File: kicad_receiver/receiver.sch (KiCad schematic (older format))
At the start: 48 parts, among them J1 Conn_01x05_Male, J2 M1+, J3 M1-, J4 M2+, J5 M2-, J6 CHG+5V, J7 CHG-, J8 BAT+, J9 BAT-, U1 LP2985-3.3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

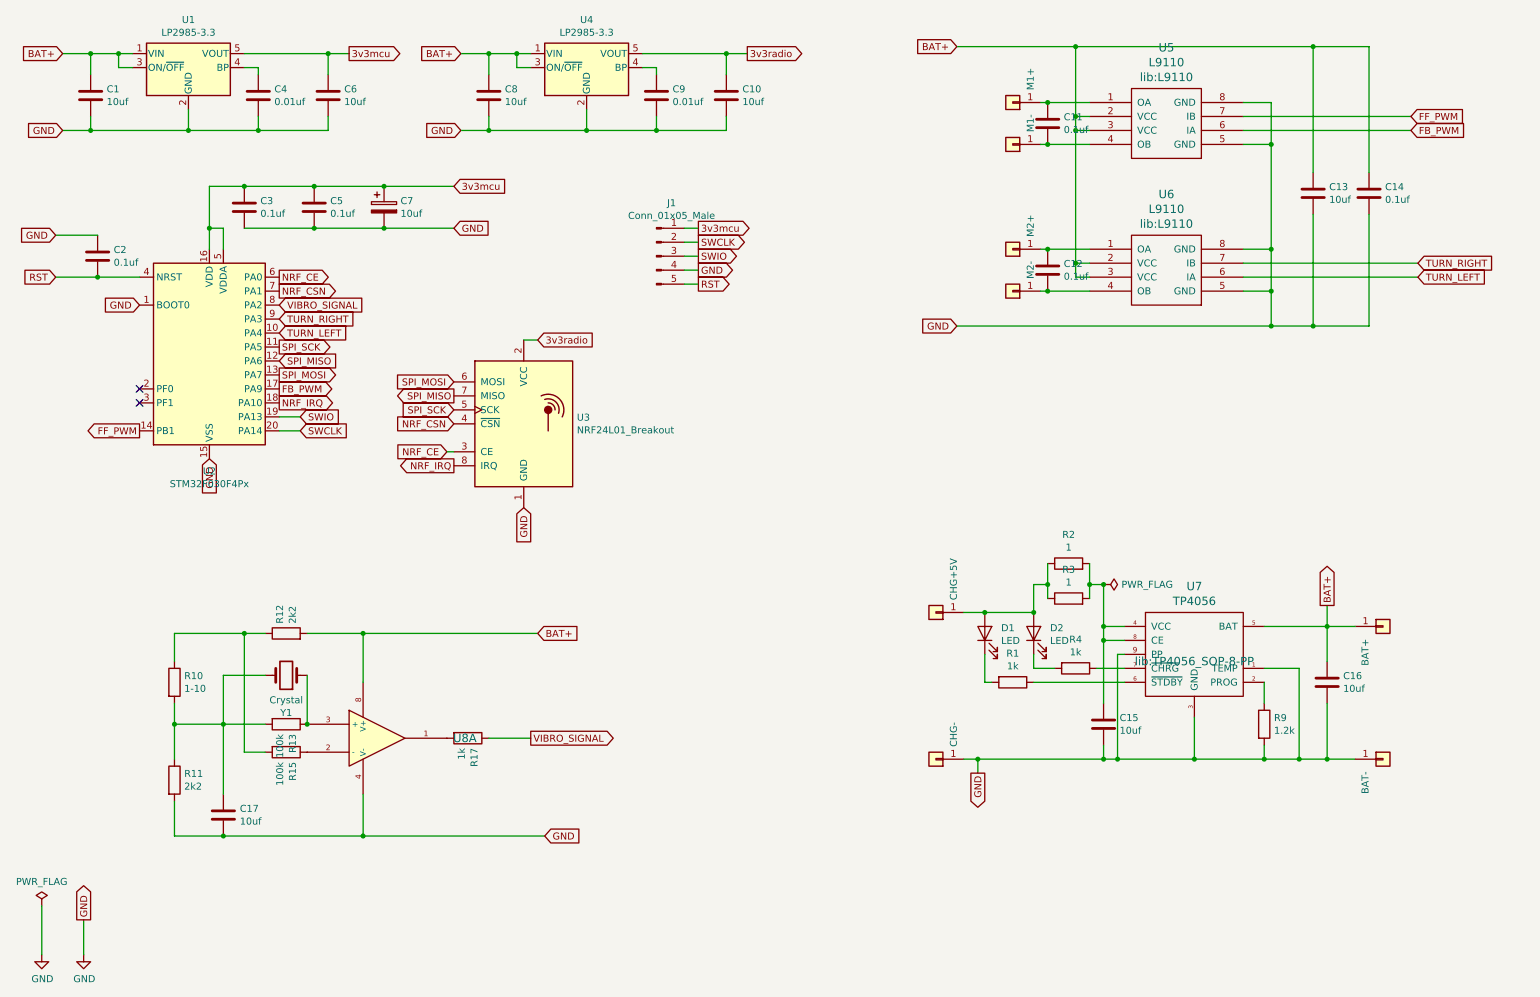
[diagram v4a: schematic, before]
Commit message: lights added, new route complete
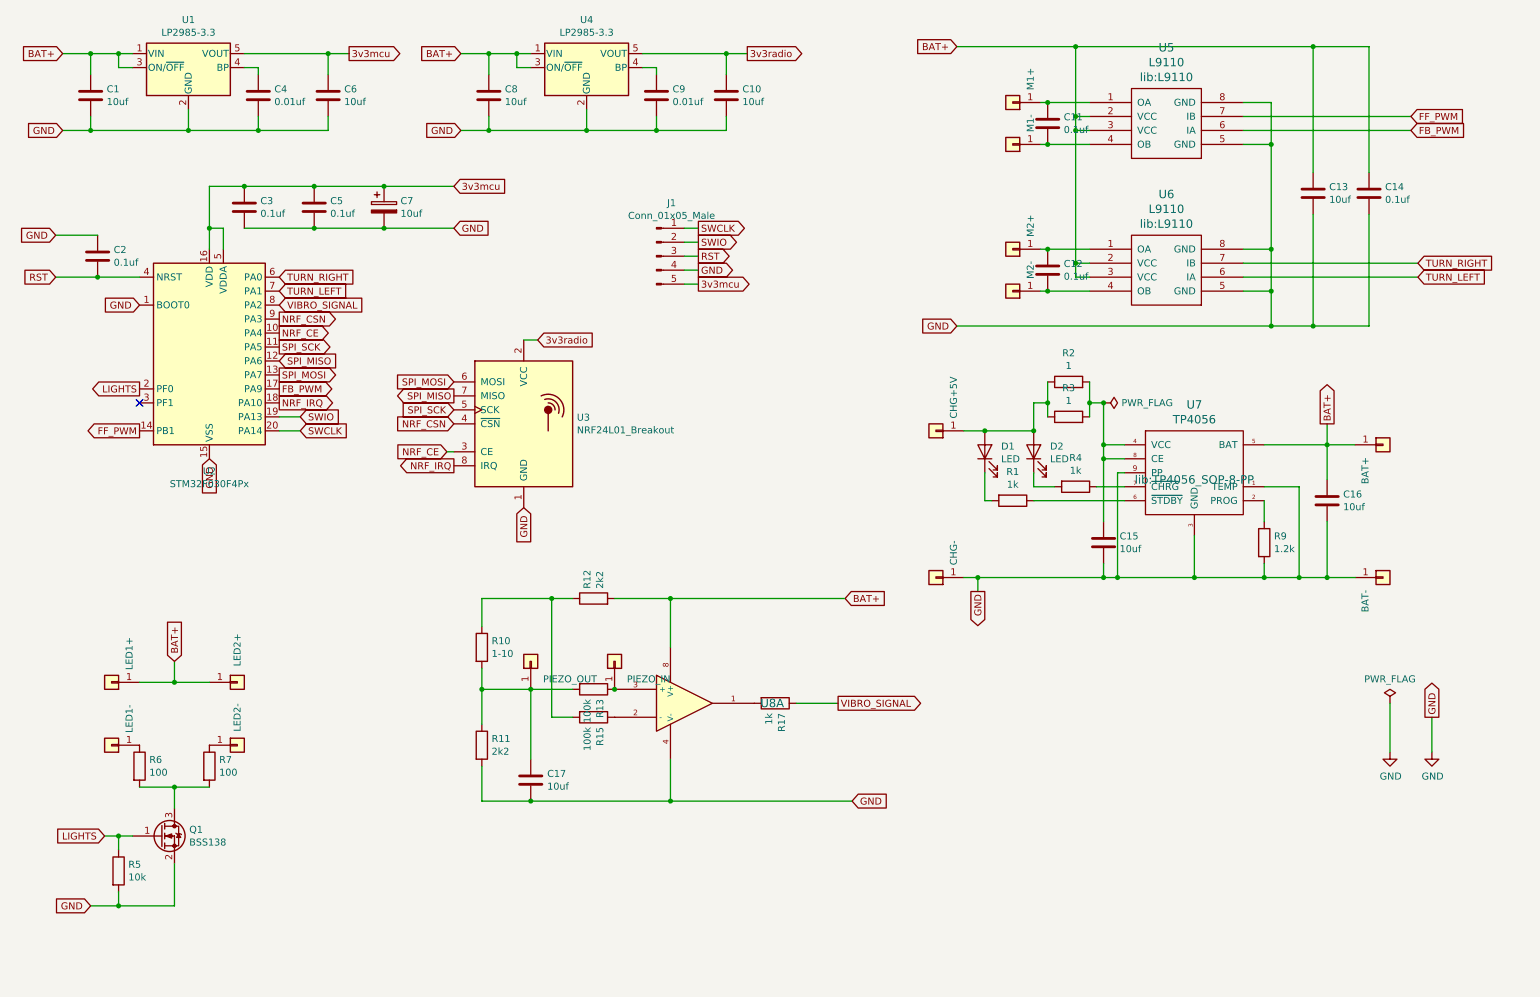
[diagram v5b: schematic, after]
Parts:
- removed Y1: Crystal, TestPoint:TestPoint_2Pads_Pitch5.08mm_Drill1.3mm, symbol Device:Crystal
- added J10: PIEZO_OUT, TestPoint:TestPoint_THTPad_4.0x4.0mm_Drill2.0mm, symbol Connector_Generic:Conn_01x01
- added J11: PIEZO_IN, TestPoint:TestPoint_THTPad_4.0x4.0mm_Drill2.0mm, symbol Connector_Generic:Conn_01x01
- added J12: LED1+, TestPoint:TestPoint_THTPad_4.0x4.0mm_Drill2.0mm, symbol Connector_Generic:Conn_01x01
- added J13: LED1-, TestPoint:TestPoint_THTPad_4.0x4.0mm_Drill2.0mm, symbol Connector_Generic:Conn_01x01
- added J14: LED2+, TestPoint:TestPoint_THTPad_4.0x4.0mm_Drill2.0mm, symbol Connector_Generic:Conn_01x01
- added J15: LED2-, TestPoint:TestPoint_THTPad_4.0x4.0mm_Drill2.0mm, symbol Connector_Generic:Conn_01x01
- added Q1: BSS138, Package_TO_SOT_SMD:SOT-23, symbol Transistor_FET:BSS138
- added R5: 10k, Resistor_SMD:R_0603_1608Metric_Pad1.05x0.95mm_HandSolder, symbol Device:R
- added R6, R7: 100, Resistor_SMD:R_0603_1608Metric_Pad1.05x0.95mm_HandSolder, symbol Device:R
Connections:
- net 3v3mcu: now also J1.5 (Pin_5); no longer J1.1 (Pin_1)
- net BAT+: now also J12.1 (Pin_1), J14.1 (Pin_1)
- net GND: now also Q1.2 (S), R5.2
- net NRF_CE: now also U2.10 (PA4); no longer U2.6 (PA0)
- net NRF_CSN: now also U2.9 (PA3); no longer U2.7 (PA1)
- net RST: now also J1.3 (Pin_3); no longer J1.5 (Pin_5)
- net SWCLK: now also J1.1 (Pin_1); no longer J1.2 (Pin_2)
- net SWIO: now also J1.2 (Pin_2); no longer J1.3 (Pin_3)
- net TURN_LEFT: now also U2.7 (PA1); no longer U2.10 (PA4)
- net TURN_RIGHT: now also U2.6 (PA0); no longer U2.9 (PA3)
- net LIGHTS: now reaches U2.2 (PF0)
- net LIGHTS: now also Q1.1 (G), R5.1
- net at R13.1, U8.3 (+): now also J11.1 (Pin_1)
- net at C17.1, R10.2, R11.1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: now also J10.1 (Pin_1)
- new net: Q1.3 (D), R6.2, R7.2
- new net: J13.1 (Pin_1), R6.1
- new net: J15.1 (Pin_1), R7.1
- no-connect marks 2 -> 1
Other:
- moved on the sheet: C15, C16, C17, D1, D2, R1, R10, R11, R12, R13, R15, R17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

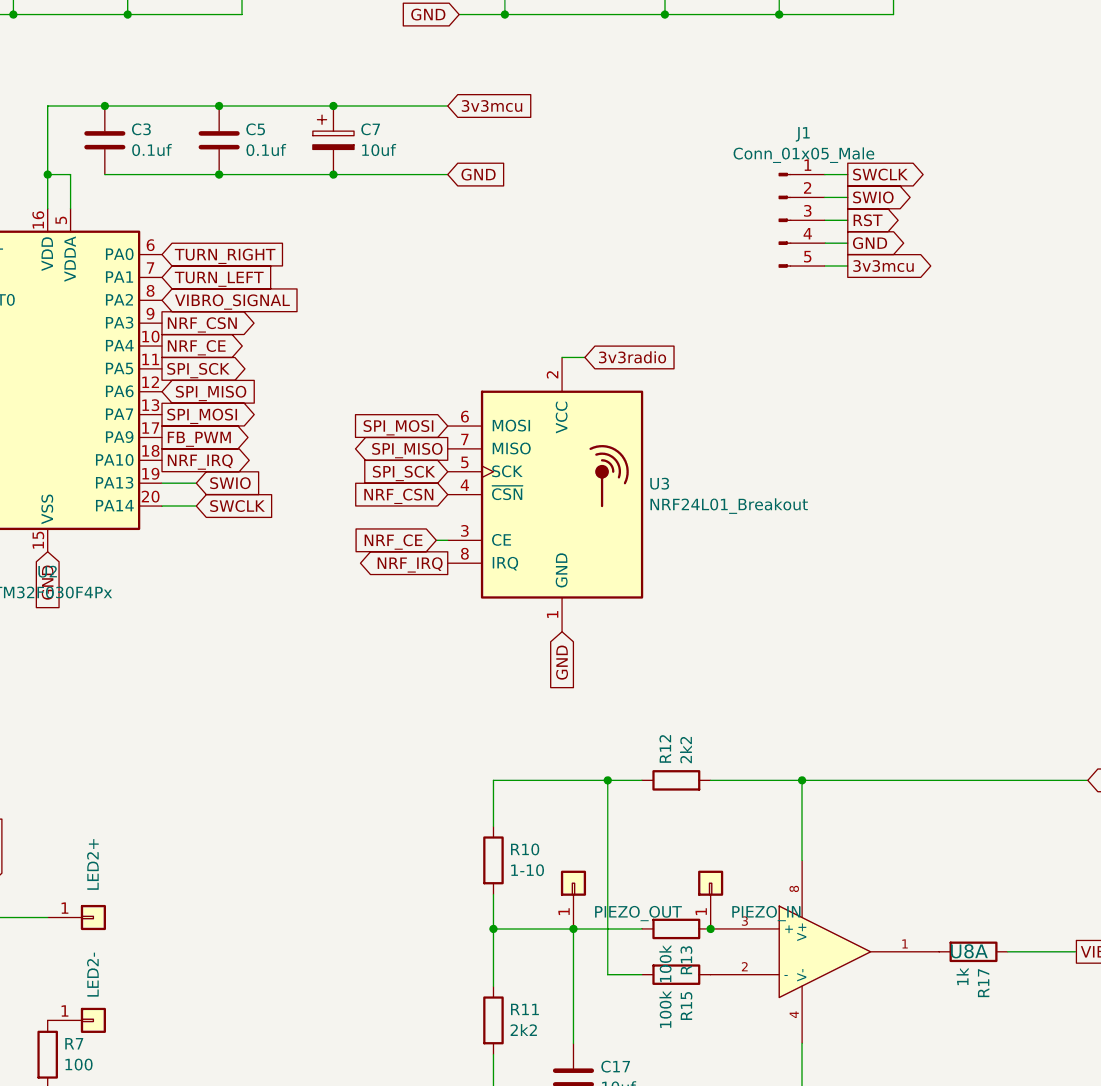
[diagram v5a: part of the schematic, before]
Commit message: layout refactored, logos added
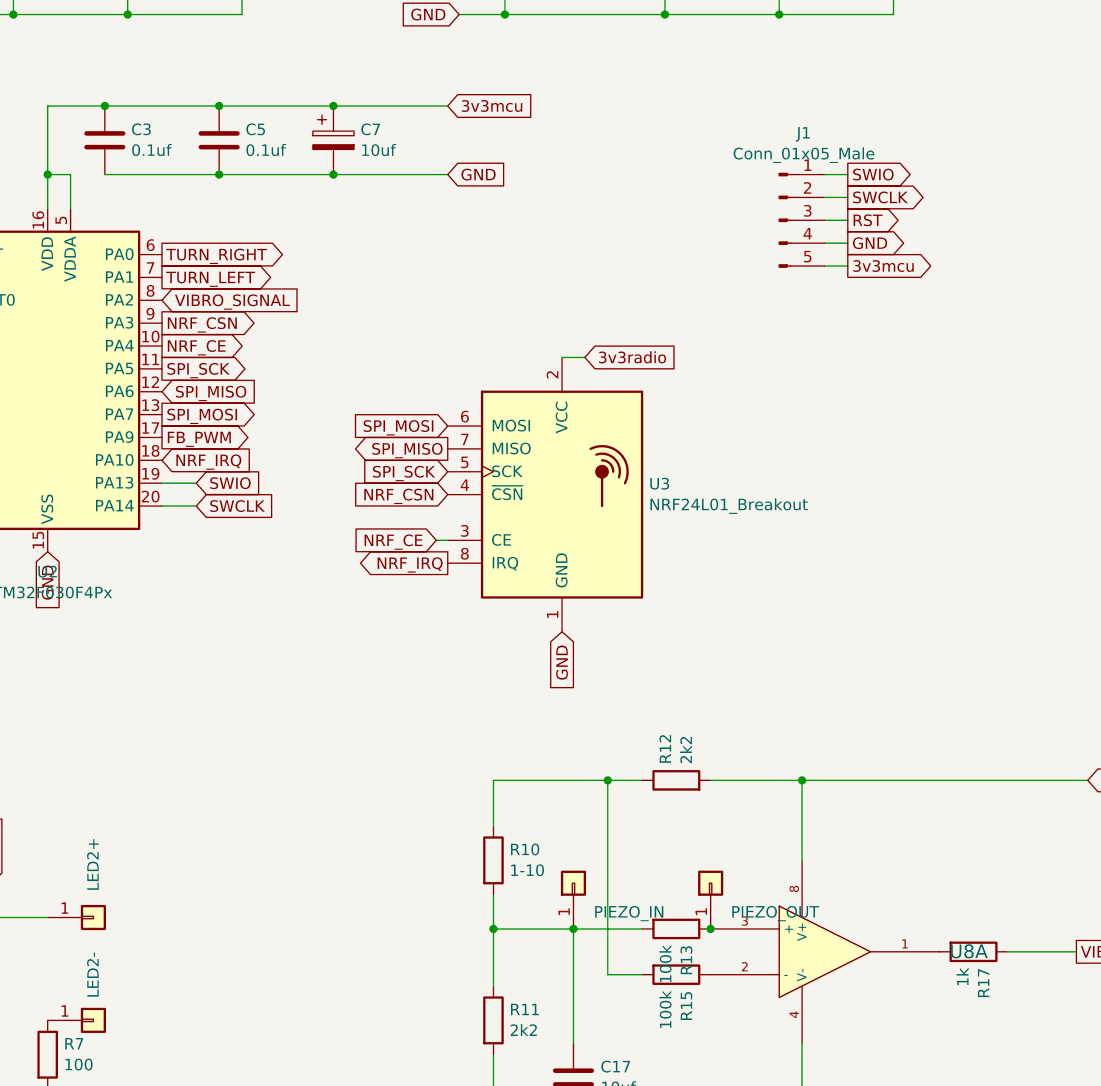
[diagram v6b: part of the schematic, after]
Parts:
- J10: value PIEZO_OUT -> PIEZO_IN
- J11: value PIEZO_IN -> PIEZO_OUT
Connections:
- net SWCLK: now also J1.2 (Pin_2); no longer J1.1 (Pin_1)
- net SWIO: now also J1.1 (Pin_1); no longer J1.2 (Pin_2)
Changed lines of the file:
@@
 	1    0    0    -1
 $EndComp
-Text GLabel 5500 2200 2    50   Output ~ 0
+Text GLabel 5500 2100 2    50   Output ~ 0
 SWIO
 Text GLabel 5500 2300 2    50   Output ~ 0
 RST
-Text GLabel 5500 2100 2    50   Output ~ 0
+Text GLabel 5500 2200 2    50   Output ~ 0
 SWCLK
 Wire Wire Line
@@
 Text GLabel 3750 3800 0    50   Output ~ 0
 NRF_IRQ
-Text GLabel 2500 3350 2    50   Output ~ 0
+Text GLabel 2500 3350 2    50   Input ~ 0
 NRF_IRQ
 Text GLabel 3700 3700 0    50   Input ~ 0
@@
 P 4300 5200
 F 0 "J10" V 4264 5112 50  0001 R CNN
-F 1 "PIEZO_OUT" V 4173 5112 50  0000 R CNN
+F 1 "PIEZO_IN" V 4173 5112 50  0000 R CNN
 F 2 "TestPoint:TestPoint_THTPad_4.0x4.0mm_Drill2.0mm" H 4300 5200 50  0001 C CNN
 F 3 "~" H 4300 5200 50  0001 C CNN
@@
 P 4900 5200
 F 0 "J11" V 4864 5112 50  0001 R CNN
-F 1 "PIEZO_IN" V 4773 5112 50  0000 R CNN
+F 1 "PIEZO_OUT" V 4773 5112 50  0000 R CNN
 F 2 "TestPoint:TestPoint_THTPad_4.0x4.0mm_Drill2.0mm" H 4900 5200 50  0001 C CNN
 F 3 "~" H 4900 5200 50  0001 C CNN
@@
 Text GLabel 2500 2850 2    50   Output ~ 0
 NRF_CE
-Text GLabel 2500 2450 2    50   Input ~ 0
+Text GLabel 2500 2450 2    50   Output ~ 0
 TURN_RIGHT
-Text GLabel 2500 2550 2    50   Input ~ 0
+Text GLabel 2500 2550 2    50   Output ~ 0
 TURN_LEFT
 $Comp
